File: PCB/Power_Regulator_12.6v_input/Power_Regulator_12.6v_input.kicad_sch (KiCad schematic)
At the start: 65 parts, among them J1 SE2-30, J10 Conn_01x01_Pin, J12 Conn_01x01_Pin, J13 Conn_01x01_Pin, J2 Jack-DC, J3 Conn_01x05_Pin, J4 Conn_01x01_Pin, J5 Conn_01x01_Pin, J6 Conn_01x01_Pin, J7 Conn_01x01_Pin, J8 Conn_01x01_Pin, J9 Conn_01x01_Pin, SW1 SW_SPDT_321, U1 TLP3542, U2 TPS55340RTER, U3 TPS563203, U4 TPS54JA20RWWR

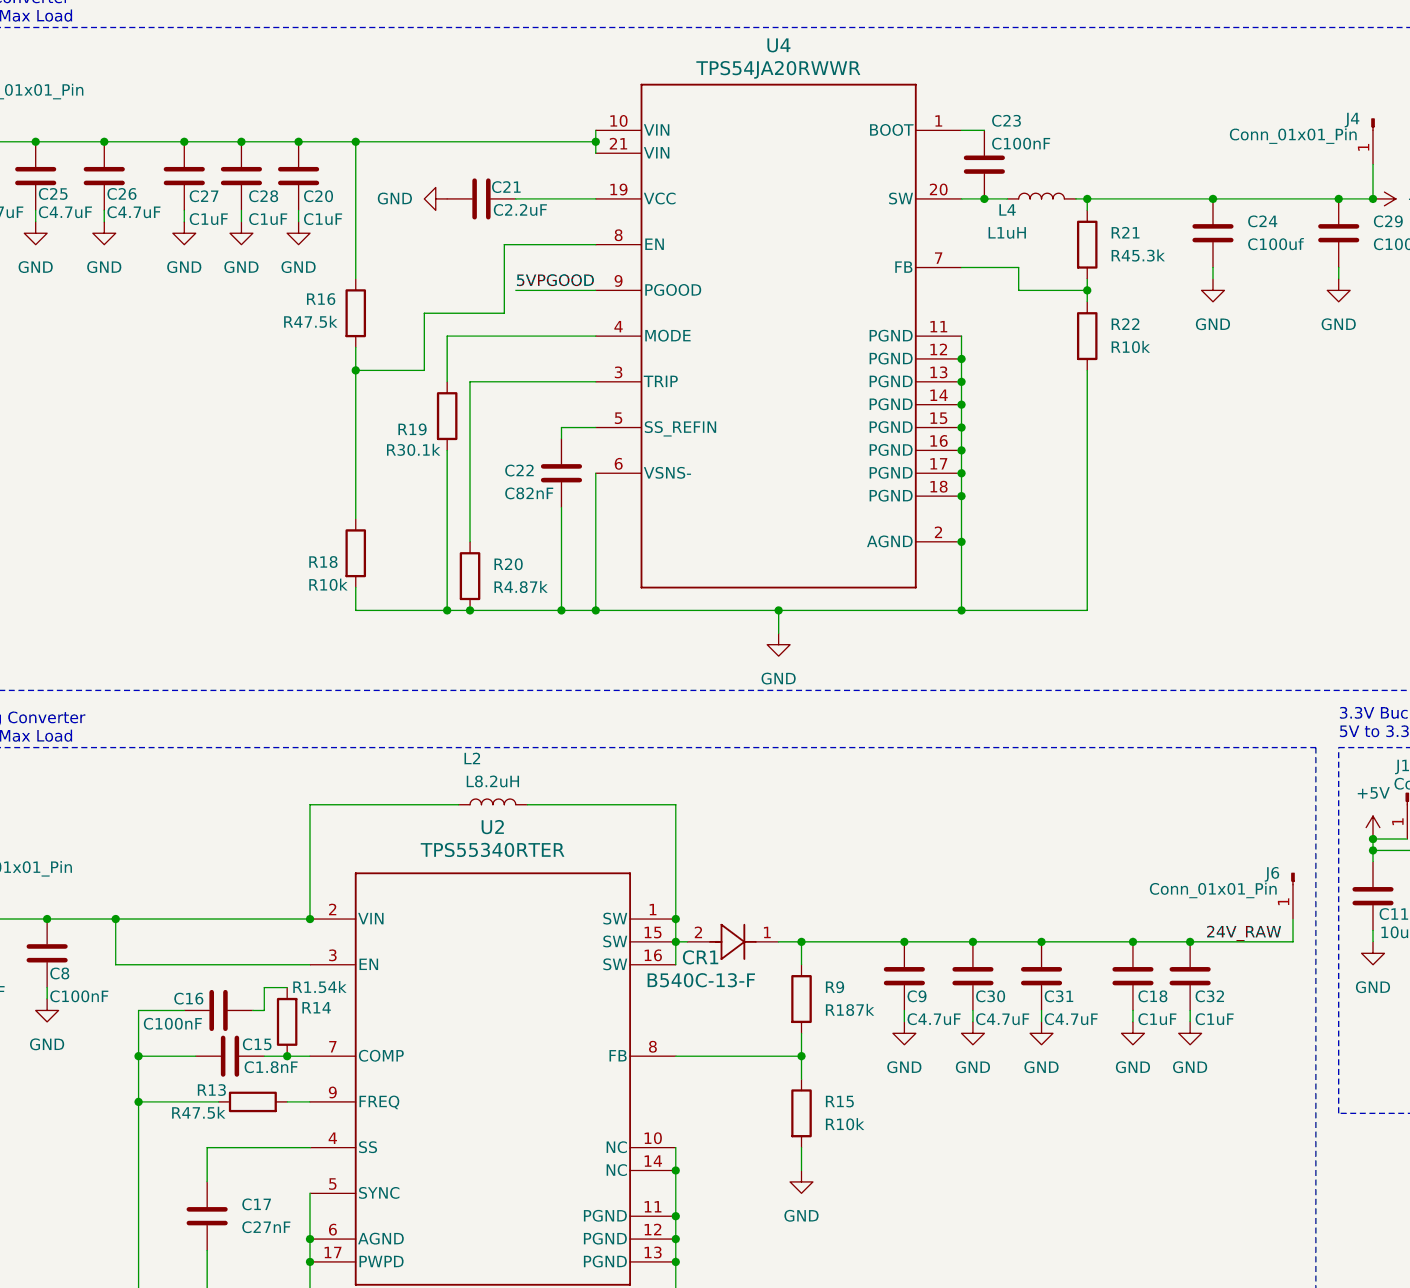
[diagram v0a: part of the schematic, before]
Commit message: updated pcb to accomodate larger inductors, fixed swapped resistors
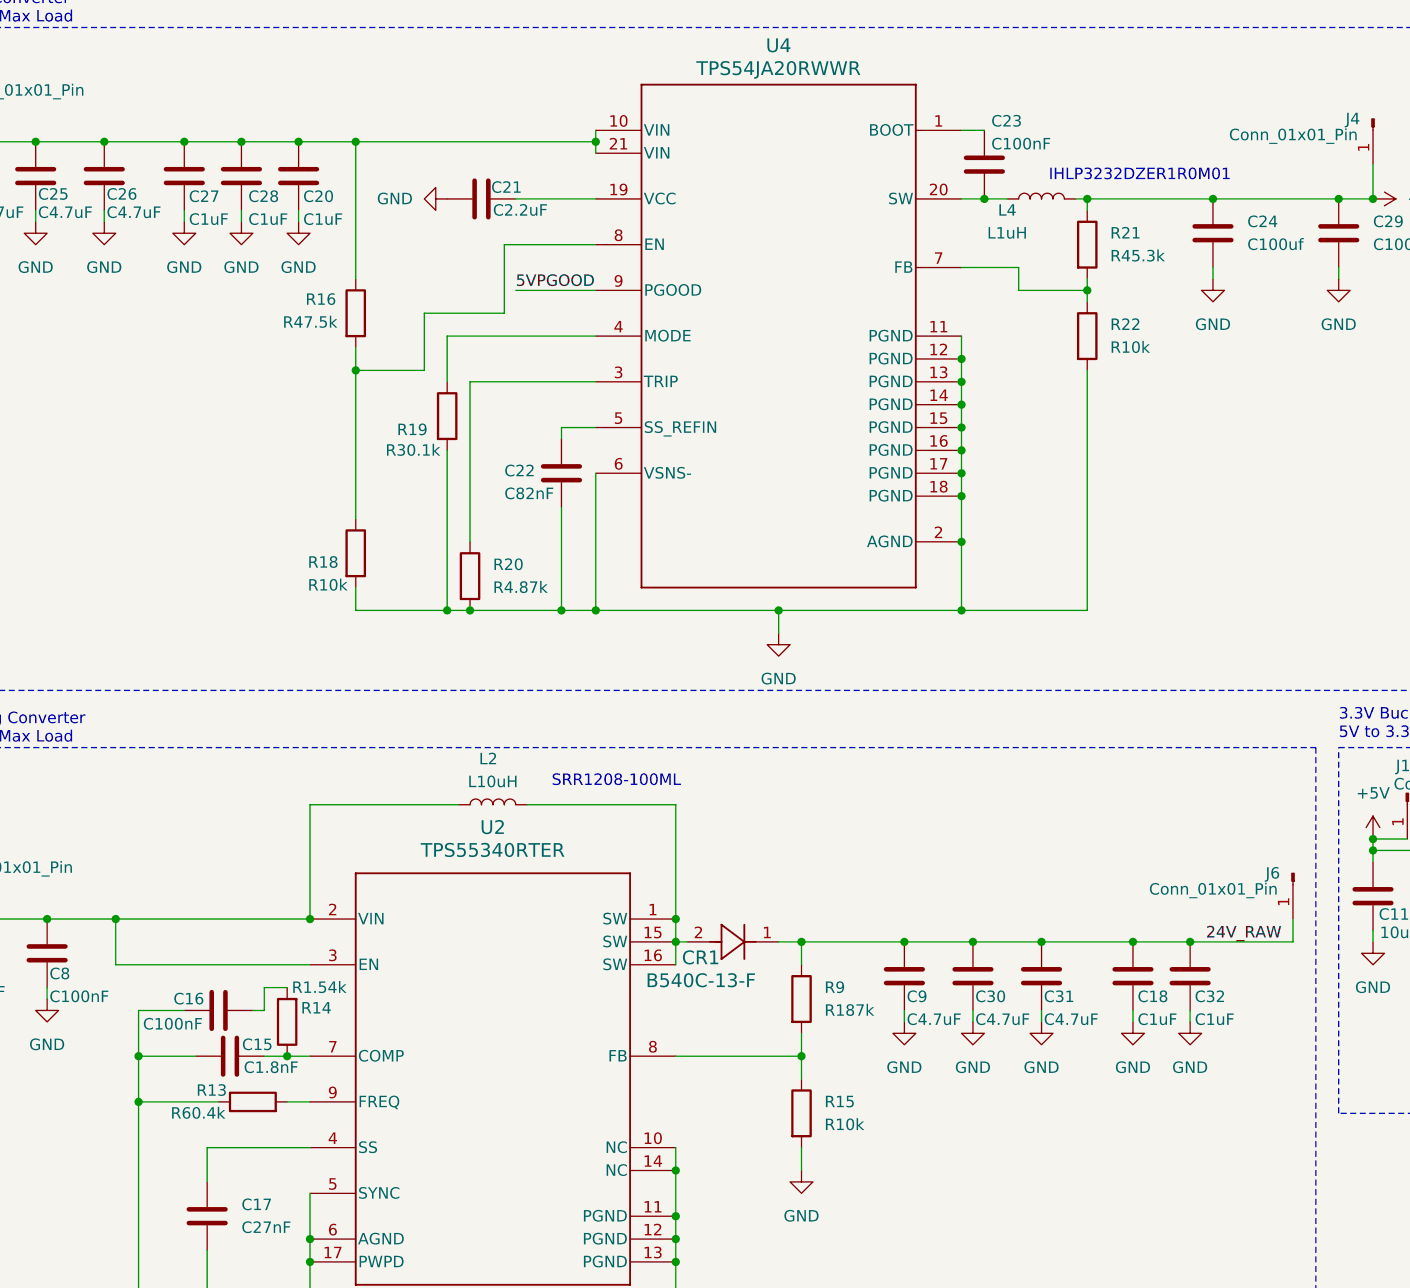
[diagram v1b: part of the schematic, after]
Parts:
- L2: value L8.2uH -> L10uH; footprint Inductor_SMD:L_0603_1608Metric -> SRR1208-100ML:IND_BOURNS_SRR1208
- L4: footprint Inductor_SMD:L_0603_1608Metric -> footprints:IND_IHLP-3232DZ_VIS-L
- R13: value R47.5k -> R60.4k
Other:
- note added: "IHLP3232DZER1R0M01"
- note added: "SRR1208-100ML"
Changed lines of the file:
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@@
 		)
 	)
+	(text "IHLP3232DZER1R0M01"
+		(exclude_from_sim no)
+		(at 156.972 34.29 0)
+		(effects
+			(font
+				(size 1.27 1.27)
+			)
+		)
+	)
 	(text "5V Buck Switching Converter\n3 18650 to 5V, 10A Max Load\n"
 		(exclude_from_sim no)
@@
 		)
 	)
+	(text "SRR1208-100ML"
+		(exclude_from_sim no)
+		(at 98.806 101.6 0)
+		(effects
+			(font
+				(size 1.27 1.27)
+			)
+		)
+	)
 	(junction
 		(at 137.16 54.61)
@@
 		(dnp no)
 		(property "Reference" "L2"
-			(at 82.804 99.06 90)
+			(at 84.582 99.06 90)
 			(effects
 				(font
@@
 			)
 		)
-		(property "Value" "L8.2uH"
+		(property "Value" "L10uH"
 			(at 85.09 101.6 90)
 			(effects
@@
 			)
 		)
-		(property "Footprint" "Inductor_SMD:L_0603_1608Metric"
+		(property "Footprint" "SRR1208-100ML:IND_BOURNS_SRR1208"
 			(at 85.09 104.14 0)
 			(effects
@@
 			)
 		)
-		(property "Value" "R47.5k"
+		(property "Value" "R60.4k"
 			(at 52.324 138.43 90)
 			(effects
@@
 			)
 		)
-		(property "Footprint" "Inductor_SMD:L_0603_1608Metric"
+		(property "Footprint" "footprints:IND_IHLP-3232DZ_VIS-L"
 			(at 146.05 36.83 0)
 			(effects
